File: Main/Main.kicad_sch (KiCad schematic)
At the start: 15 parts, among them J2 Fires, M1 ServoHandL, M2 ServoHandR, M3 ServoRotateFry, M4 ServoFixFry, M5 MotorLT, M6 MotorLB, M7 MotorRT, M8 MotorRB, Q1 2SC1815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

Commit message: up main
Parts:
- added BT1: MotorBattery, Connector_PinHeader_2.54mm:PinHeader_1x02_P2.54mm_Vertical, symbol Device:Battery_Cell
- added J1: AdvancedConnector1, Connector_PinSocket_2.54mm:PinSocket_1x06_P2.54mm_Vertical, symbol Connector:Conn_01x06_Socket
- added J3: Conn_01x08_Socket, Connector_PinSocket_2.54mm:PinSocket_1x08_P2.54mm_Vertical, symbol Connector:Conn_01x08_Socket
- M4: footprint (none) -> Connector_PinSocket_2.54mm:PinSocket_1x03_P2.54mm_Vertical
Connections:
- net Fire: now also U1.8 (GPIO6/TOUCH6/ADC1_CH5)
- net GND: no longer U3.3 (PGND), U3.4 (PGND), U3.5 (PGND), U4.3 (PGND), U4.4 (PGND), U4.5 (PGND)
- net L_AI_1: now also U1.25 (GPIO21)
- net L_AI_2: now also U1.26 (GPIO26)
- net L_AI_P: now also U1.27 (GPIO33)
- net L_BI_1: now also U1.24 (GPIO20/U1CTS/ADC2_CH9/CLK_OUT1/USB_D+)
- net L_BI_2: now also U1.23 (GPIO19/U1RTS/ADC2_CH8/CLK_OUT2/USB_D-)
- net L_BI_P: now also U1.22 (GPIO18/U1RXD/ADC2_CH7/DAC_2/CLK_OUT3/RGB_LED)
- net PWM_FixFry: now also U1.37 (U0TXD/GPIO43/CLK_OUT1)
- net PWM_HandL: now also U1.34 (MTDO/JTAG/GPIO40)
- net PWM_HandR: now also U1.35 (MTDI/JTAG/GPIO41)
- net PWM_RotateFry: now also U1.36 (MTMS/JTAG/GPIO42)
- net R_AI_1: now also U1.31 (GPIO37)
- net R_AI_2: now also U1.32 (GPIO38)
- net R_AI_P: now also U1.33 (MTCK/JTAG/GPIO39)
- net R_BI_1: now also U1.30 (GPIO36)
- net R_BI_2: now also U1.29 (GPIO35)
- net R_BI_P: now also U1.28 (GPIO34)
- net VCCQ: now also BT1.1 (+)
- net DF_RX: now reaches U1.10 (GPIO8/TOUCH8/ADC1_CH7)
- net DF_RX: now also U2.2 (RX)
- net at U1.11 (GPIO9/TOUCH9/ADC1_CH8/FSPIHD): now also J3.1 (Pin_1)
- net at U1.12 (GPIO10/TOUCH10/ADC1_CH9/FSPICS0/FSPIIO4): now also J3.2 (Pin_2)
- net at U1.13 (GPIO11/TOUCH11/ADC2_CH0/FSPID/FSPIIO5): now also J3.3 (Pin_3)
- net at U1.14 (GPIO12/TOUCH12/ADC2_CH1/FSPICLK/FSPIIO6): now also J3.4 (Pin_4)
- net at U1.15 (GPIO13/TOUCH13/ADC2_CH2/FSPIQ/FSPIIO7): now also J3.5 (Pin_5)
- net at U1.16 (GPIO14/TOUCH14/ADC2_CH3/FSPIWP/FSPIDQS): now also J3.6 (Pin_6)
- net GPIO15: now reaches U1.17 (GPIO15/U0RTS/ADC2_CH4/XTAL_32K_P)
- net GPIO15: now also J3.7 (Pin_7)
- net GPIO16: now reaches U1.18 (GPIO16/U0CTS/ADC2_CH5/XTAL_32K_N)
- net GPIO16: now also J3.8 (Pin_8)
- net at U1.2 (GPIO0/BOOT): now also J1.1 (Pin_1)
- net at U1.3 (GPIO1/TOUCH1/ADC1_CH0): now also J1.2 (Pin_2)
- net at U1.4 (GPIO2/TOUCH2/ADC1_CH1): now also J1.3 (Pin_3)
- net at U1.5 (GPIO3/TOUCH3/ADC1_CH2): now also J1.4 (Pin_4)
- net at U1.6 (GPIO4/TOUCH4/ADC1_CH3): now also J1.5 (Pin_5)
- net at U1.7 (GPIO5/TOUCH5/ADC1_CH4): now also J1.6 (Pin_6)
- net DF_TX: now reaches U1.9 (GPIO7/TOUCH7/ADC1_CH6)
- net DF_TX: now also U2.3 (TX)
- new net GND1: BT1.2 (-), U3.3 (PGND), U3.4 (PGND), U3.5 (PGND), U4.3 (PGND), U4.4 (PGND), U4.5 (PGND)
- no-connect marks 0 -> 15

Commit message: センサー関係忘れてた
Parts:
- added J4, J5: Conn_01x02_Socket, Connector_PinSocket_2.54mm:PinSocket_1x02_P2.54mm_Vertical, symbol Connector:Conn_01x02_Socket
- BT1, J2, M5, M6, M7, M8: footprint Connector_PinHeader_2.54mm:PinHeader_1x02_P2.54mm_Vertical -> Connector_PinSocket_2.54mm:PinSocket_1x02_P2.54mm_Vertical
- M4: footprint Connector_PinSocket_2.54mm:PinSocket_1x03_P2.54mm_Vertical -> Connector_PinHeader_2.54mm:PinHeader_1x03_P2.54mm_Vertical
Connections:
- net GND: now also J5.1 (Pin_1), J5.2 (Pin_2)
- net VCC: now also J4.1 (Pin_1)
- net GPIO17: now reaches U1.19 (GPIO17/U1TXD/ADC2_CH6/DAC_1)
- net GPIO17: now also J4.2 (Pin_2)
- no-connect marks 15 -> 14
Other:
- moved on the sheet: J3

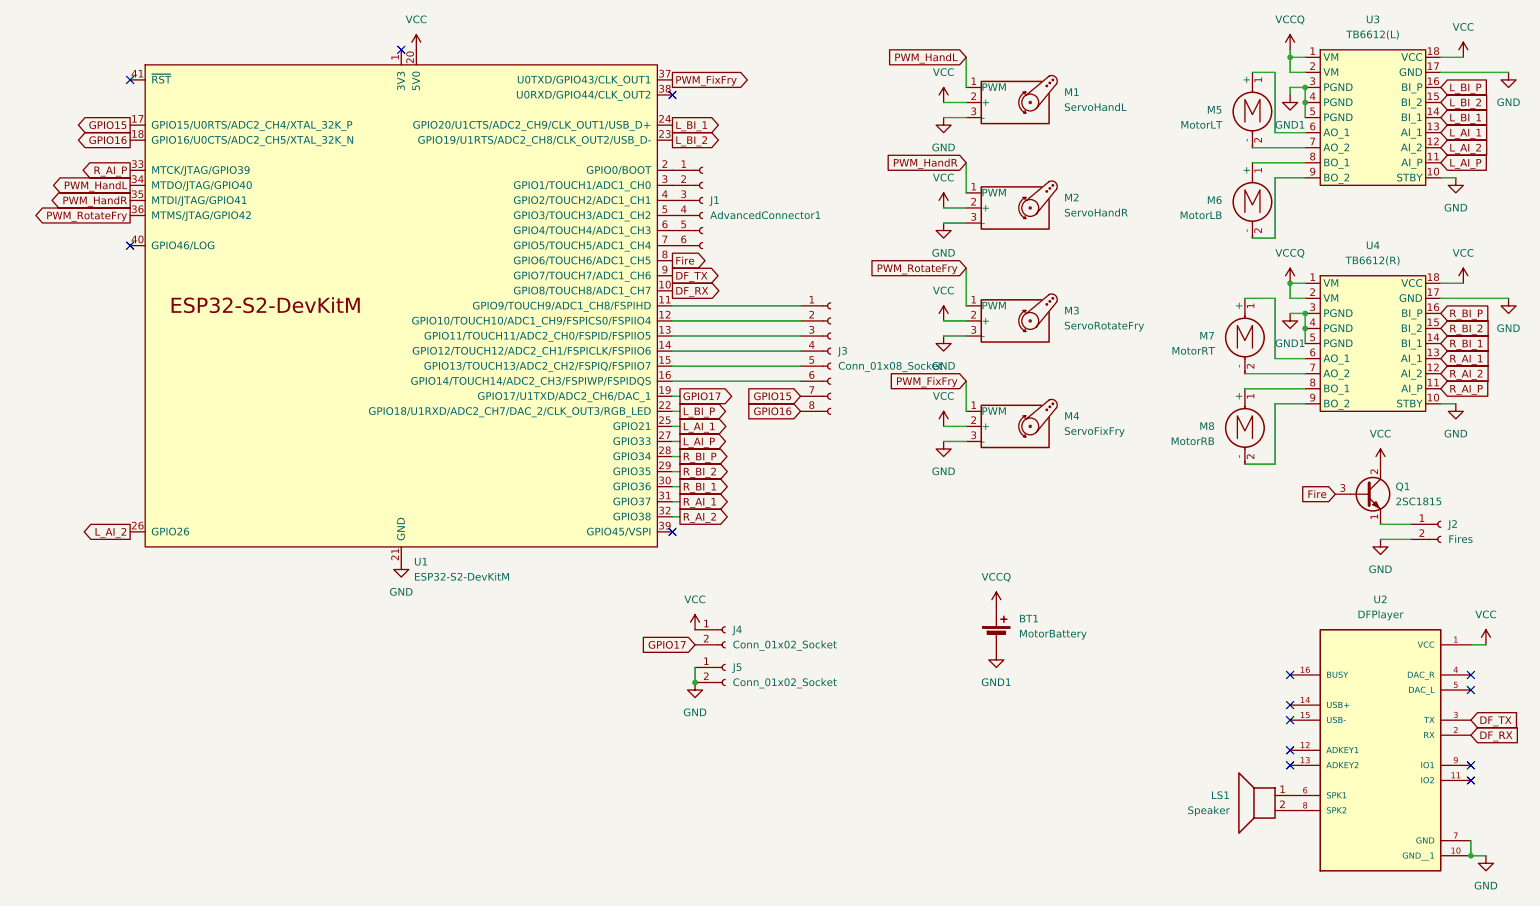
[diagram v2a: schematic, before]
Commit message: 出力を追加
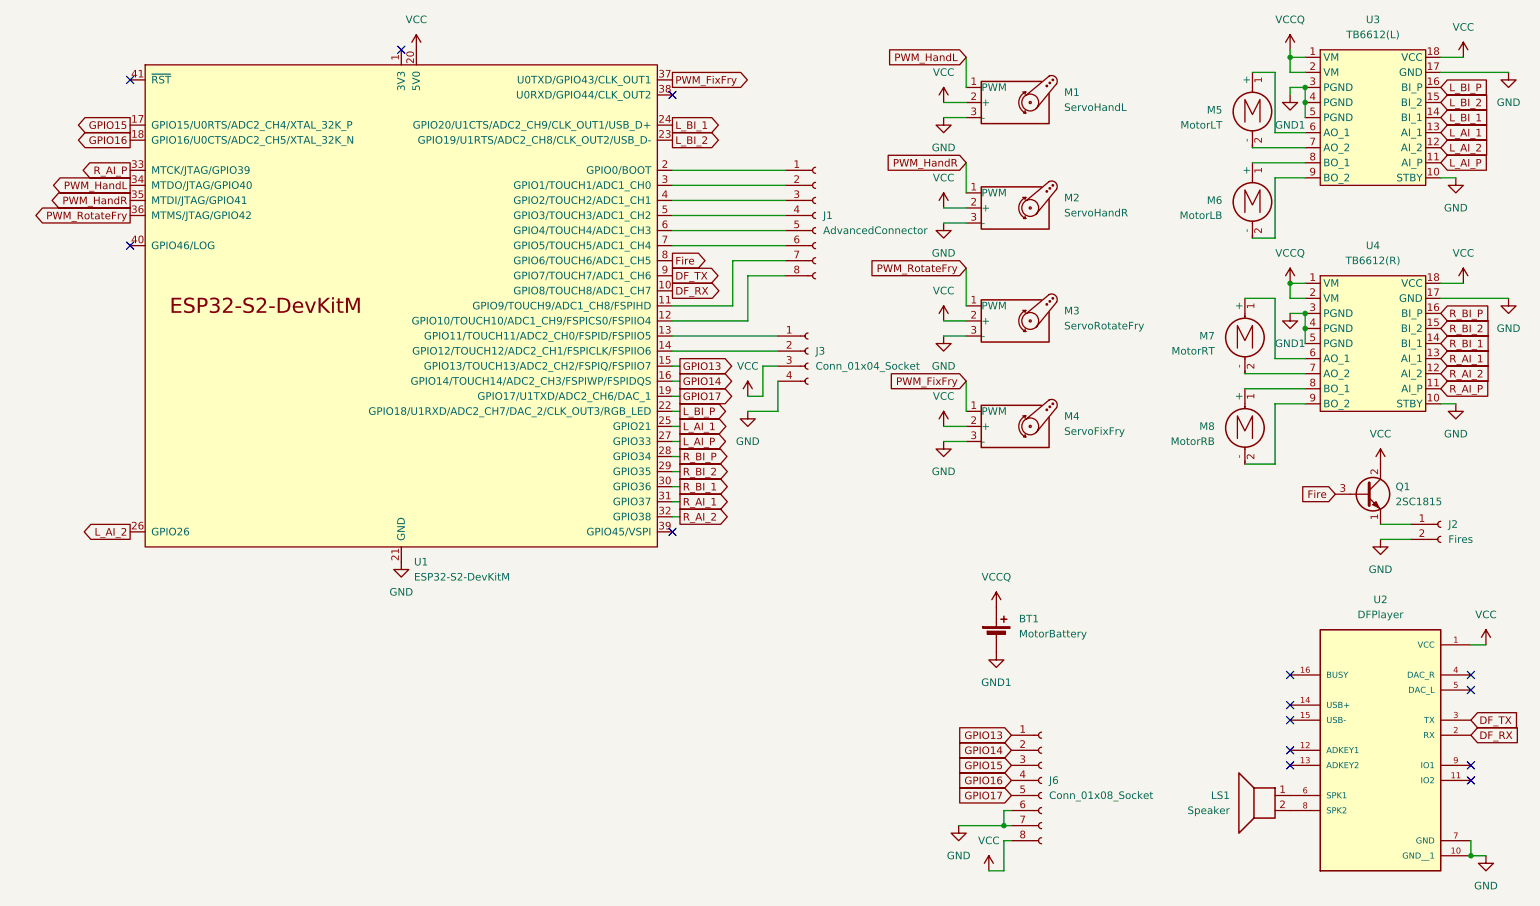
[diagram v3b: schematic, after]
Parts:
- removed J1: AdvancedConnector1, Connector_PinSocket_2.54mm:PinSocket_1x06_P2.54mm_Vertical, symbol Connector:Conn_01x06_Socket
- removed J3: Conn_01x08_Socket, Connector_PinSocket_2.54mm:PinSocket_1x08_P2.54mm_Vertical, symbol Connector:Conn_01x08_Socket
- removed J4, J5: Conn_01x02_Socket, Connector_PinSocket_2.54mm:PinSocket_1x02_P2.54mm_Vertical, symbol Connector:Conn_01x02_Socket
- added J1: AdvancedConnector, Connector_PinSocket_2.54mm:PinSocket_1x08_P2.54mm_Vertical, symbol Connector:Conn_01x08_Socket
- added J3: Conn_01x04_Socket, Connector_PinSocket_2.54mm:PinSocket_1x04_P2.54mm_Vertical, symbol Connector:Conn_01x04_Socket
- added J6: Conn_01x08_Socket, Connector_PinSocket_2.54mm:PinSocket_1x08_P2.54mm_Vertical, symbol Connector:Conn_01x08_Socket
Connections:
- net GND: now also J3.4 (Pin_4), J6.6 (Pin_6), J6.7 (Pin_7)
- net GPIO15: now also J6.3 (Pin_3)
- net GPIO16: now also J6.4 (Pin_4)
- net GPIO17: now also J6.5 (Pin_5)
- net VCC: now also J3.3 (Pin_3), J6.8 (Pin_8)
- net at U1.11 (GPIO9/TOUCH9/ADC1_CH8/FSPIHD): now also J1.7 (Pin_7)
- net at U1.12 (GPIO10/TOUCH10/ADC1_CH9/FSPICS0/FSPIIO4): now also J1.8 (Pin_8)
- net at U1.13 (GPIO11/TOUCH11/ADC2_CH0/FSPID/FSPIIO5): now also J3.1 (Pin_1)
- net at U1.14 (GPIO12/TOUCH12/ADC2_CH1/FSPICLK/FSPIIO6): now also J3.2 (Pin_2)
- net GPIO13: now reaches U1.15 (GPIO13/TOUCH13/ADC2_CH2/FSPIQ/FSPIIO7)
- net GPIO13: now also J6.1 (Pin_1)
- net GPIO14: now reaches U1.16 (GPIO14/TOUCH14/ADC2_CH3/FSPIWP/FSPIDQS)
- net GPIO14: now also J6.2 (Pin_2)
- net at U1.2 (GPIO0/BOOT): now also J1.1 (Pin_1)
- net at U1.3 (GPIO1/TOUCH1/ADC1_CH0): now also J1.2 (Pin_2)
- net at U1.4 (GPIO2/TOUCH2/ADC1_CH1): now also J1.3 (Pin_3)
- net at U1.5 (GPIO3/TOUCH3/ADC1_CH2): now also J1.4 (Pin_4)
- net at U1.6 (GPIO4/TOUCH4/ADC1_CH3): now also J1.5 (Pin_5)
- net at U1.7 (GPIO5/TOUCH5/ADC1_CH4): now also J1.6 (Pin_6)
